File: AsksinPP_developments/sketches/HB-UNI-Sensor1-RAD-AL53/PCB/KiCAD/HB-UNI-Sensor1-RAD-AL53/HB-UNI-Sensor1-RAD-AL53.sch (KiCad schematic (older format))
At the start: 49 parts, among them J1 Conn_01x02_Male, J10 Conn_01x06, J2 Conn_01x04, J3 Conn_01x04, J4 Conn_01x02, J5 Conn_01x02, J6 Conn_01x02, J7 Conn_01x02, J8 Conn_01x04, J9 Conn_01x04, Q1 IRLU024N, SW1 Config Button

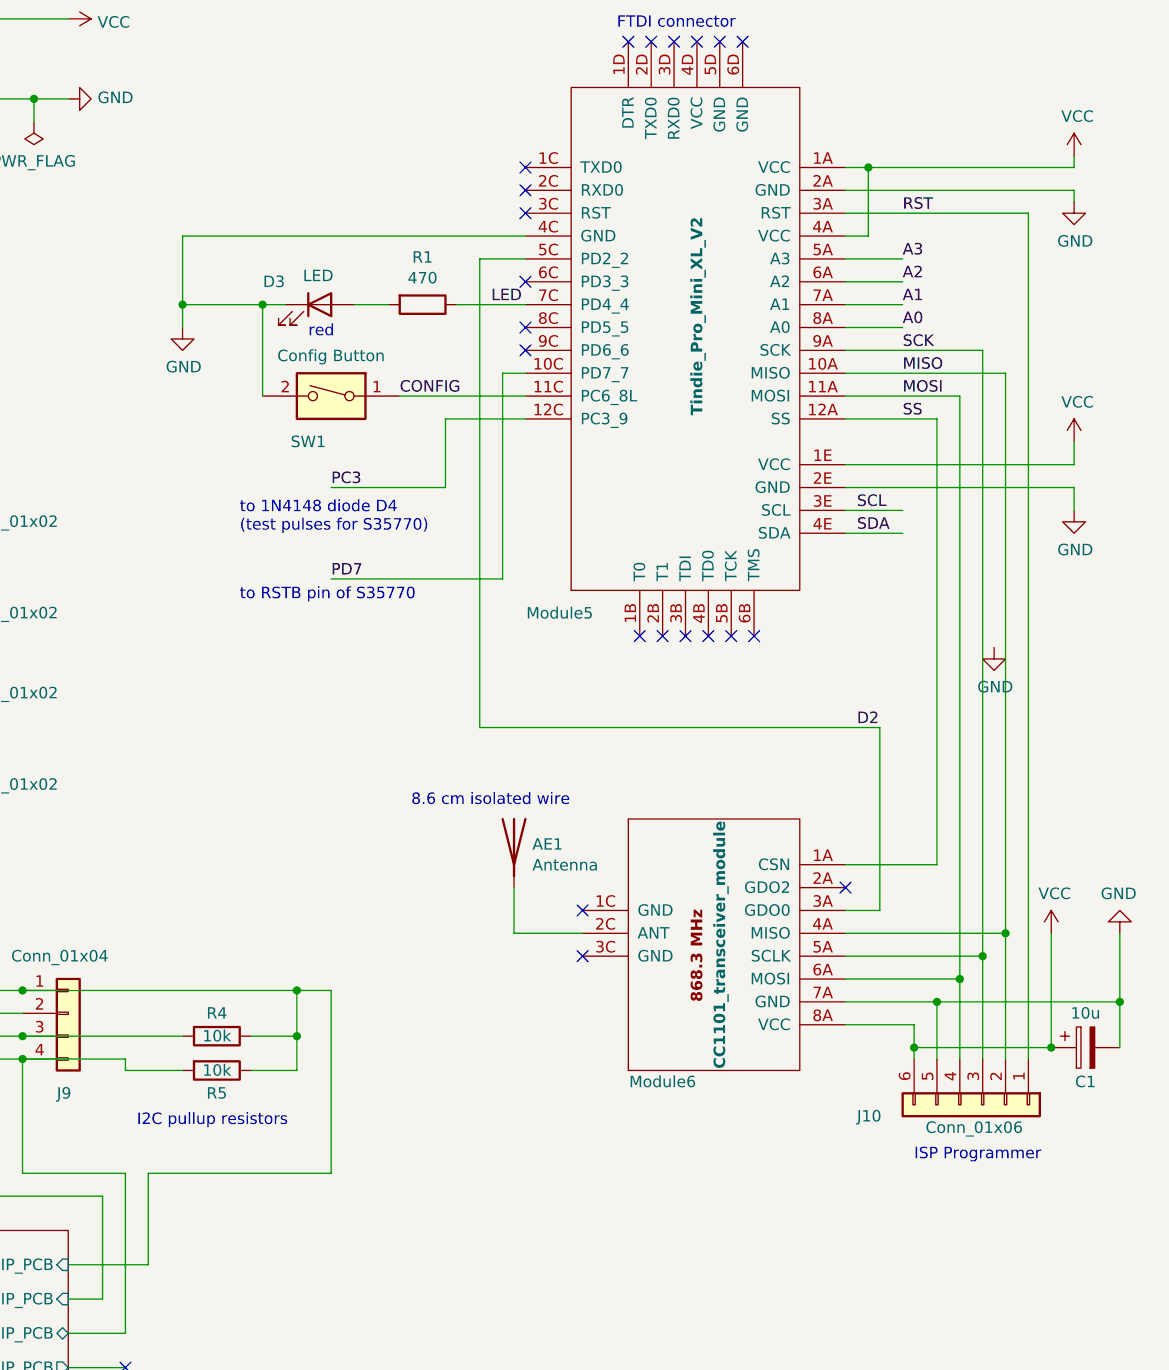
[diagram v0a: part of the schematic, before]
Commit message: added pre-release of HB-UNI-SEN-BATT_FUEL4EP (still under test!)
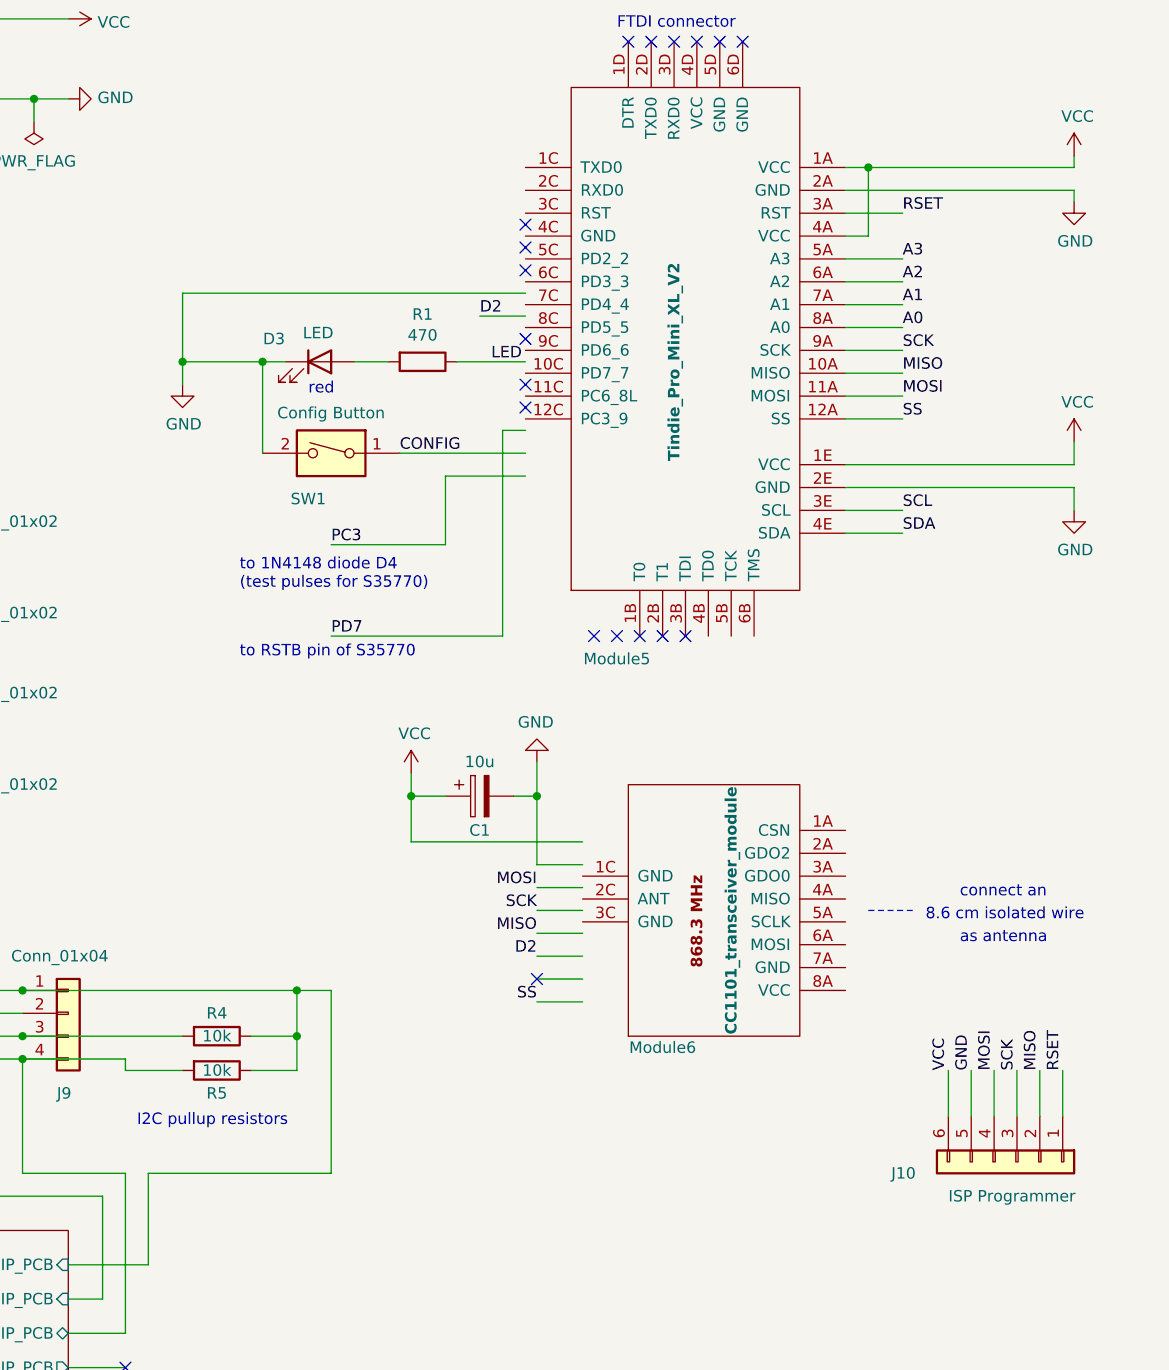
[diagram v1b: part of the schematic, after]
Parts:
- removed AE1: Antenna, symbol Device:Antenna
- J10: value Conn_01x06 -> ISP Programmer
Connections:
- net labels added: RSET
- net labels removed: RST
- wire segments 252 -> 244
- no-connect marks 26 -> 23
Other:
- note added: "as antenna"
- note added: "connect an"
- note removed: "ISP Programmer"
- moved on the sheet: C1, D3, J10, Module6, R1, SW1
